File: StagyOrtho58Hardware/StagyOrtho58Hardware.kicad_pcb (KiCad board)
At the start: 2 copper layers, 73 parts, among them J11 USB_C_Receptacle, SW11 SW_Push, SW12 SW_Push, SW13 SW_Push, SW14 SW_Push, SW15 SW_Push, SW16 SW_Push, SW17 SW_Push, SW18 SW_Push, SW19 SW_Push, SW20 SW_Push, SW21 SW_Push, SW22 SW_Push, SW23 SW_Push, SW24 SW_Push, SW25 SW_Push, SW26 SW_Push, SW27 SW_Push, SW28 SW_Push, SW29 SW_Push, SW30 SW_Push, SW31 SW_Push, SW32 SW_Push, SW33 SW_Push, SW34 SW_Push, SW35 SW_Push, SW36 SW_Push, SW37 SW_Push, SW38 SW_Push, SW39 SW_Push, SW40 SW_Push, U11 Pico, U12 MCP23S17_ML

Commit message: Comfortable positions of the keys, ready to layout
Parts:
- J11: value USB_C_Receptacle -> USB_C_Receptacle_USB2.0
- SW29: footprint Switch_Keyboard_Kailh:SW_Kailh_Choc_V1V2_1.50u -> Switch_Keyboard_Kailh:SW_Kailh_Choc_V1V2_2.00u
- SW35: footprint Switch_Keyboard_Kailh:SW_Kailh_Choc_V1V2_1.50u -> Switch_Keyboard_Kailh:SW_Kailh_Choc_V1V2_1.00u
- SW38: footprint Switch_Keyboard_Kailh:SW_Kailh_Choc_V1V2_1.50u_90deg -> Switch_Keyboard_Kailh:SW_Kailh_Choc_V1V2_1.50u
- SW39: footprint Switch_Keyboard_Kailh:SW_Kailh_Choc_V1V2_2.00u -> Switch_Keyboard_Kailh:SW_Kailh_Choc_V1V2_1.00u
- moved SW34 69.9 mm to (144.1, 135.4)
- moved SW30 42.8 mm to (153.7, 112.0)
- moved SW38 36.6 mm to (233.2, 145.8), turned to 35 degrees
- moved SW39 30.0 mm to (231.1, 105.9)
- moved SW37 28.3 mm to (222.8, 130.8), turned to 35 degrees
- moved SW35 26.0 mm to (170.2, 135.4)
- moved SW36 24.8 mm to (194.9, 135.4)
- moved SW31 23.7 mm to (172.7, 108.2)
- moved SW32 21.9 mm to (191.8, 114.3)
- moved SW33 21.0 mm to (210.8, 111.5)
- moved SW29 16.3 mm to (120.4, 117.1)
- moved J11 12.6 mm to (55.9, 99.7)
- moved SW11 11.7 mm to (115.6, 62.2)
- moved SW17 7.08 mm to (111.0, 80.5)
- moved SW23 6.93 mm to (111.0, 98.8)
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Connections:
- J11 pad A5: unconnected-(J11-PadA5) -> /~{RESET}
- J11 pad A8: unconnected-(J11-PadA8) -> Net-(U12-Pad15)
- J11 pad B5: unconnected-(J11-PadB5) -> /GREEN
- J11 pad B8: unconnected-(J11-PadB8) -> Net-(U12-Pad16)
- U12 pad 14: Net-(J11-PadA3) -> /~{RESET}
- U12 pad 15: Net-(J11-PadB10) -> Net-(U12-Pad15)
- U12 pad 16: Net-(J11-PadB11) -> Net-(U12-Pad16)

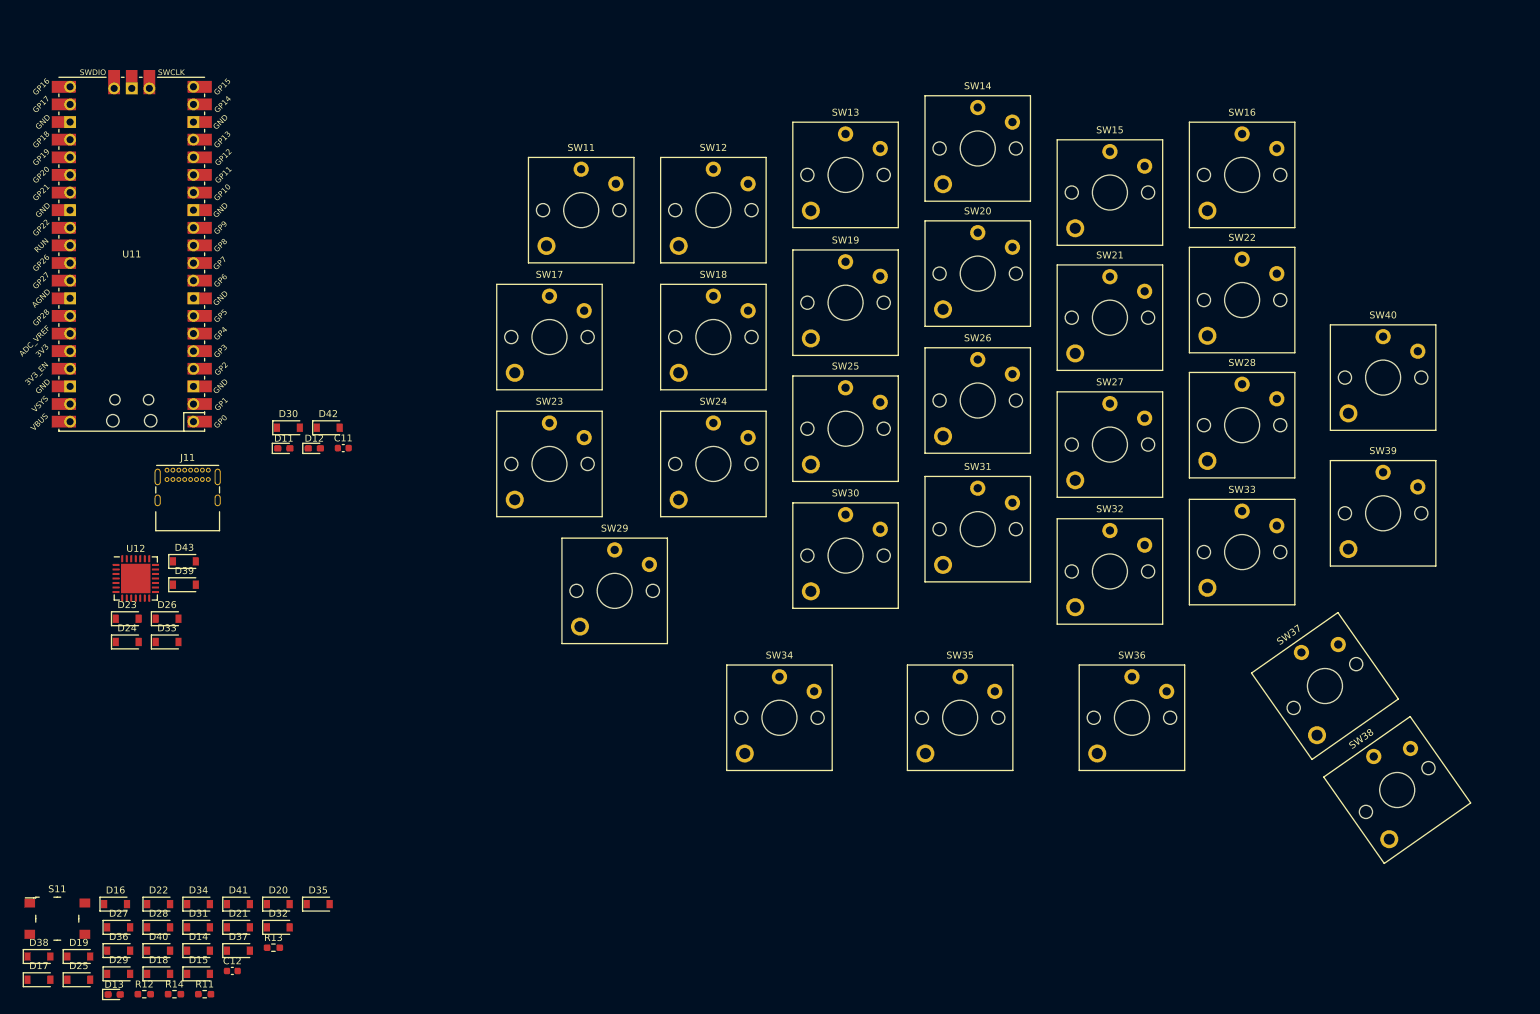
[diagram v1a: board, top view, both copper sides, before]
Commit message: Placed all components, board outline added
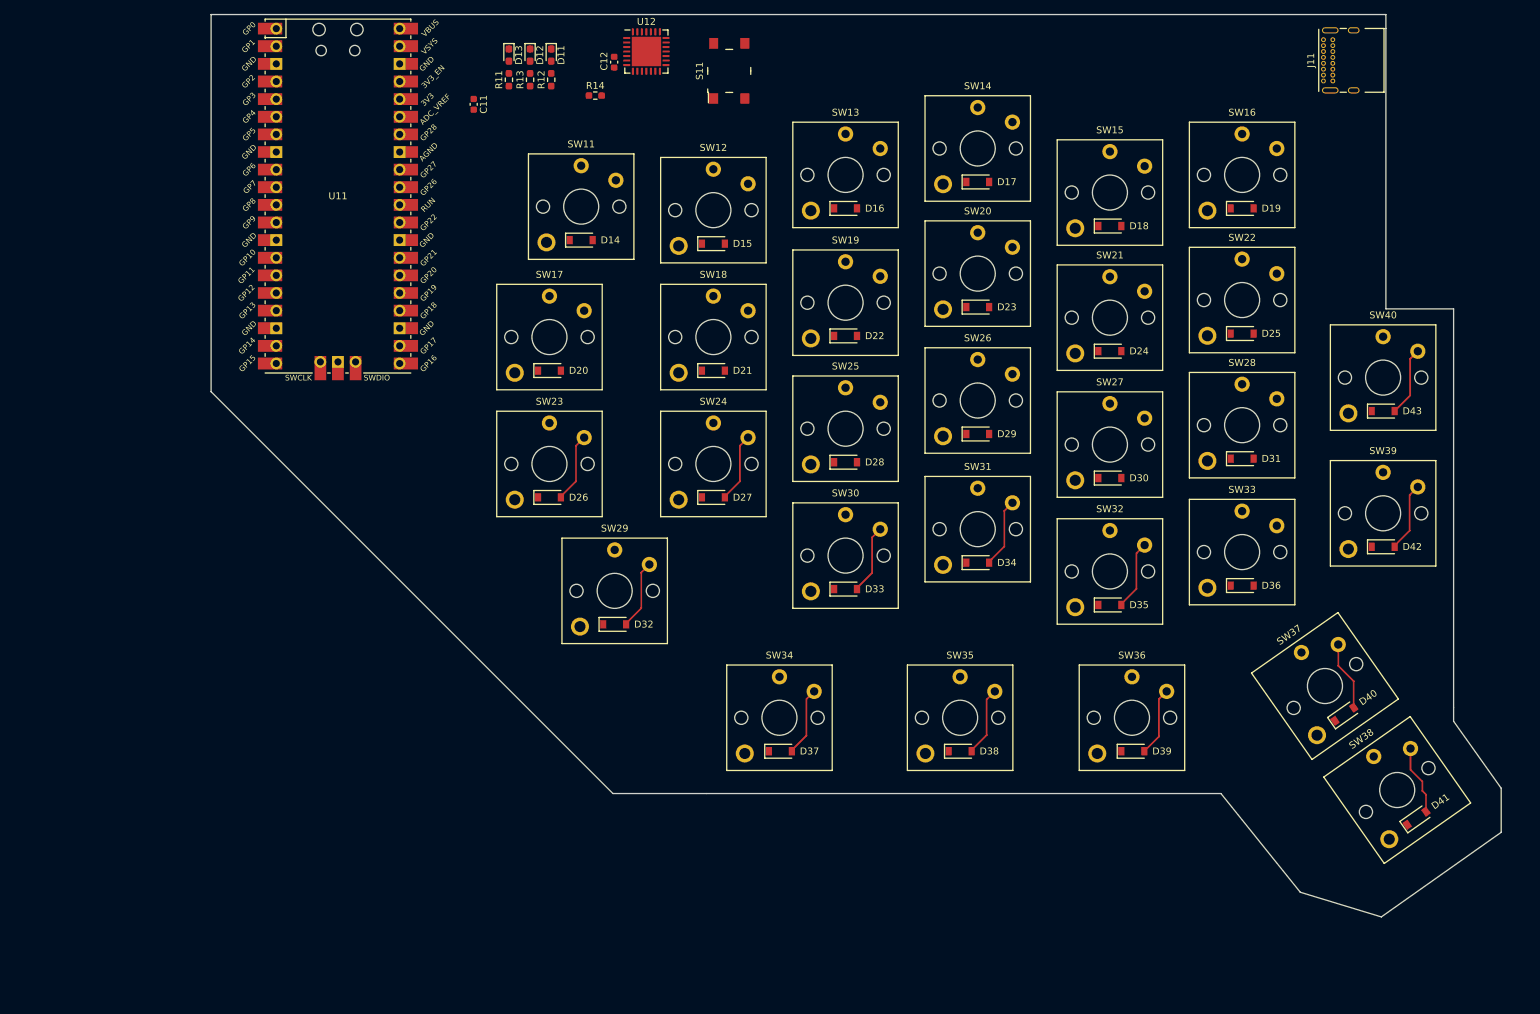
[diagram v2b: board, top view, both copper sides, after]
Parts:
- SW37, SW38: footprint Switch_Keyboard_Kailh:SW_Kailh_Choc_V1V2_1.50u -> Switch_Keyboard_Kailh:SW_Kailh_Choc_V1V2_1.00u
- moved D19 199.3 mm to (210.8, 62.0)
- moved D25 191.8 mm to (210.8, 80.0)
- moved D17 177.6 mm to (172.7, 58.2)
- moved J11 175.8 mm to (222.5, 43.6), turned to 90 degrees
- moved D18 174.4 mm to (191.8, 64.5)
- moved D40 174.2 mm to (225.6, 134.9), turned to 35 degrees
- moved D43 174.1 mm to (231.1, 91.2)
- moved D41 170.3 mm to (236.0, 149.9), turned to 35 degrees
- moved D36 170.2 mm to (210.8, 116.3)
- moved D31 164.9 mm to (210.8, 98.0)
- moved S11 155.9 mm to (136.9, 42.2), turned to 90 degrees
- moved D42 153.0 mm to (231.1, 110.7)
- moved D24 147.7 mm to (191.8, 82.5)
- moved D13 146.9 mm to (105.2, 39.9), turned to -90 degrees
- moved D29 146.2 mm to (172.7, 94.5)
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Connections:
- net Net-(U12-Pad15) renamed /INTB
- net Net-(U12-Pad16) renamed /INTA
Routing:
- net Net-(D41-Pad2): track 0.00 -> 10.0 mm
- net Net-(D40-Pad2): track 0.00 -> 10.0 mm
- net Net-(D35-Pad2): track 0.00 -> 10.0 mm
- net Net-(D26-Pad2): track 0.00 -> 10.0 mm
- net Net-(D42-Pad2): track 0.00 -> 10.0 mm
- net Net-(D38-Pad2): track 0.00 -> 10.0 mm
- net Net-(D34-Pad2): track 0.00 -> 10.0 mm
- net Net-(D33-Pad2): track 0.00 -> 10.0 mm
- net Net-(D32-Pad2): track 0.00 -> 10.0 mm
- net Net-(D43-Pad2): track 0.00 -> 10.0 mm
- net Net-(D27-Pad2): track 0.00 -> 10.0 mm
- net Net-(D37-Pad2): track 0.00 -> 9.96 mm
- net Net-(D39-Pad2): track 0.00 -> 9.96 mm
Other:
- board outline added: 185.9 x 130 mm

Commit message: Partial routing complete, approx 40%
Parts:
- added H11: MountingHole, MountingHole:MountingHole_3.2mm_M3, F.Cu at (66.0, 86.4)
- added H12: MountingHole, MountingHole:MountingHole_3.2mm_M3, F.Cu at (123.0, 140.4)
- added H13: MountingHole, MountingHole:MountingHole_3.2mm_M3, F.Cu at (236.4, 119.6)
- added H14: MountingHole, MountingHole:MountingHole_3.2mm_M3, F.Cu at (157.9, 38.2)
- added H15: MountingHole, MountingHole:MountingHole_3.2mm_M3, F.Cu at (226.6, 51.9)
- added H16: MountingHole, MountingHole:MountingHole_3.2mm_M3, F.Cu at (65.7, 37.8)
- added H17: MountingHole, MountingHole:MountingHole_2.7mm_M2.5, F.Cu at (207.2, 124.3)
- added H18: MountingHole, MountingHole:MountingHole_2.7mm_M2.5, F.Cu at (122.7, 73.9)
- added H19: MountingHole, MountingHole:MountingHole_2.7mm_M2.5, F.Cu at (168.3, 85.4)
- added H20: MountingHole, MountingHole:MountingHole_2.7mm_M2.5, F.Cu at (171.7, 121.0)
- SW37: footprint Switch_Keyboard_Kailh:SW_Kailh_Choc_V1V2_1.00u -> Switch_Keyboard_Kailh:SW_Kailh_Choc_V1V2_1.50u
- moved D37 9.74 mm to (154.0, 139.8)
- moved SW34 9.74 mm to (153.9, 135.0)
- moved D41 4.58 mm to (232.7, 153.1)
- moved SW38 4.58 mm to (229.9, 149.0)
- moved SW35 4.50 mm to (174.7, 135.0)
- moved D38 4.50 mm to (174.7, 139.8)
- moved SW37 1.10 mm to (221.7, 131.1)
- moved D40 1.10 mm to (224.5, 135.2)
- moved U11 1.08 mm to (81.6, 60.2)
- moved SW36 0.49 mm to (195.2, 135.0)
- moved D39 0.49 mm to (195.3, 139.8)
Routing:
- net /ROW_4: track 0.00 -> 135.6 mm
- net /ROW_3: track 0.00 -> 132.4 mm
- net /ROW_2: track 0.00 -> 122.4 mm
- net /ROW_1: track 0.00 -> 122.0 mm
- net /ROW_0: track 0.00 -> 118.6 mm
- net /COL_0: track 0.00 -> 72.2 mm
- net /COL_5: track 0.00 -> 62.5 mm
- net /COL_2: track 0.00 -> 42.6 mm
- net /COL_1: track 0.00 -> 42.6 mm
- net /COL_4: track 0.00 -> 42.3 mm
- net /COL_3: track 0.00 -> 42.2 mm
- net Net-(D18-Pad2): track 0.00 -> 10.0 mm
- net Net-(D24-Pad2): track 0.00 -> 10.0 mm
- net Net-(D30-Pad2): track 0.00 -> 10.0 mm
- net Net-(D29-Pad2): track 0.00 -> 10.0 mm
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
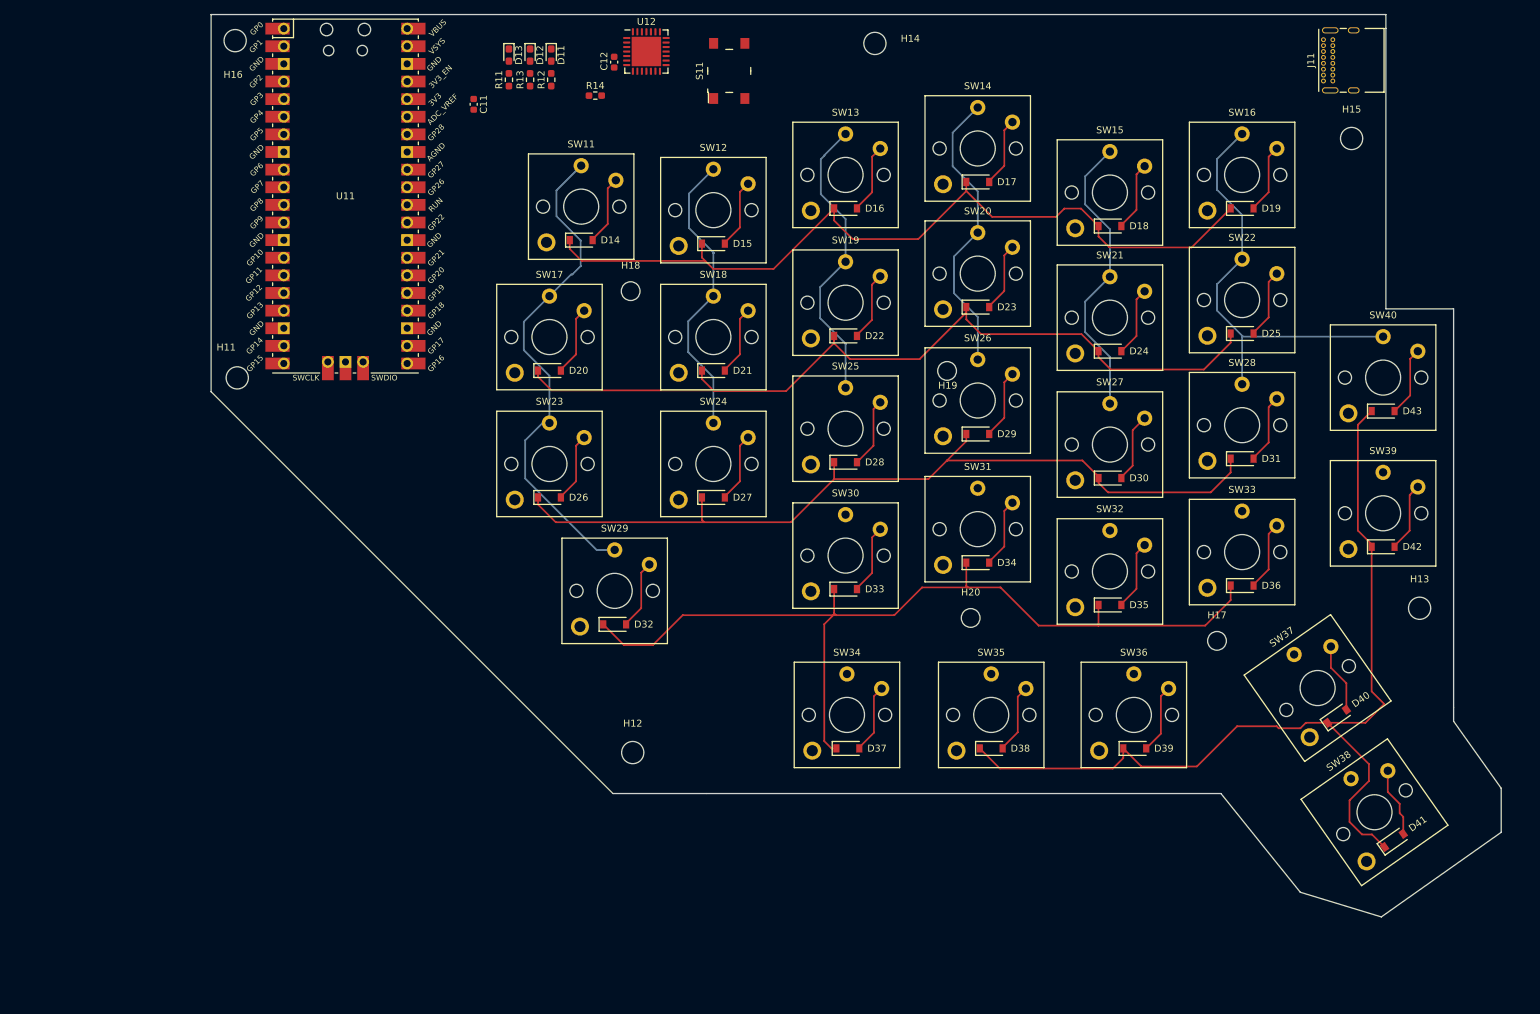
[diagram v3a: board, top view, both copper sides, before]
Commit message: Routes rows, columns in switches
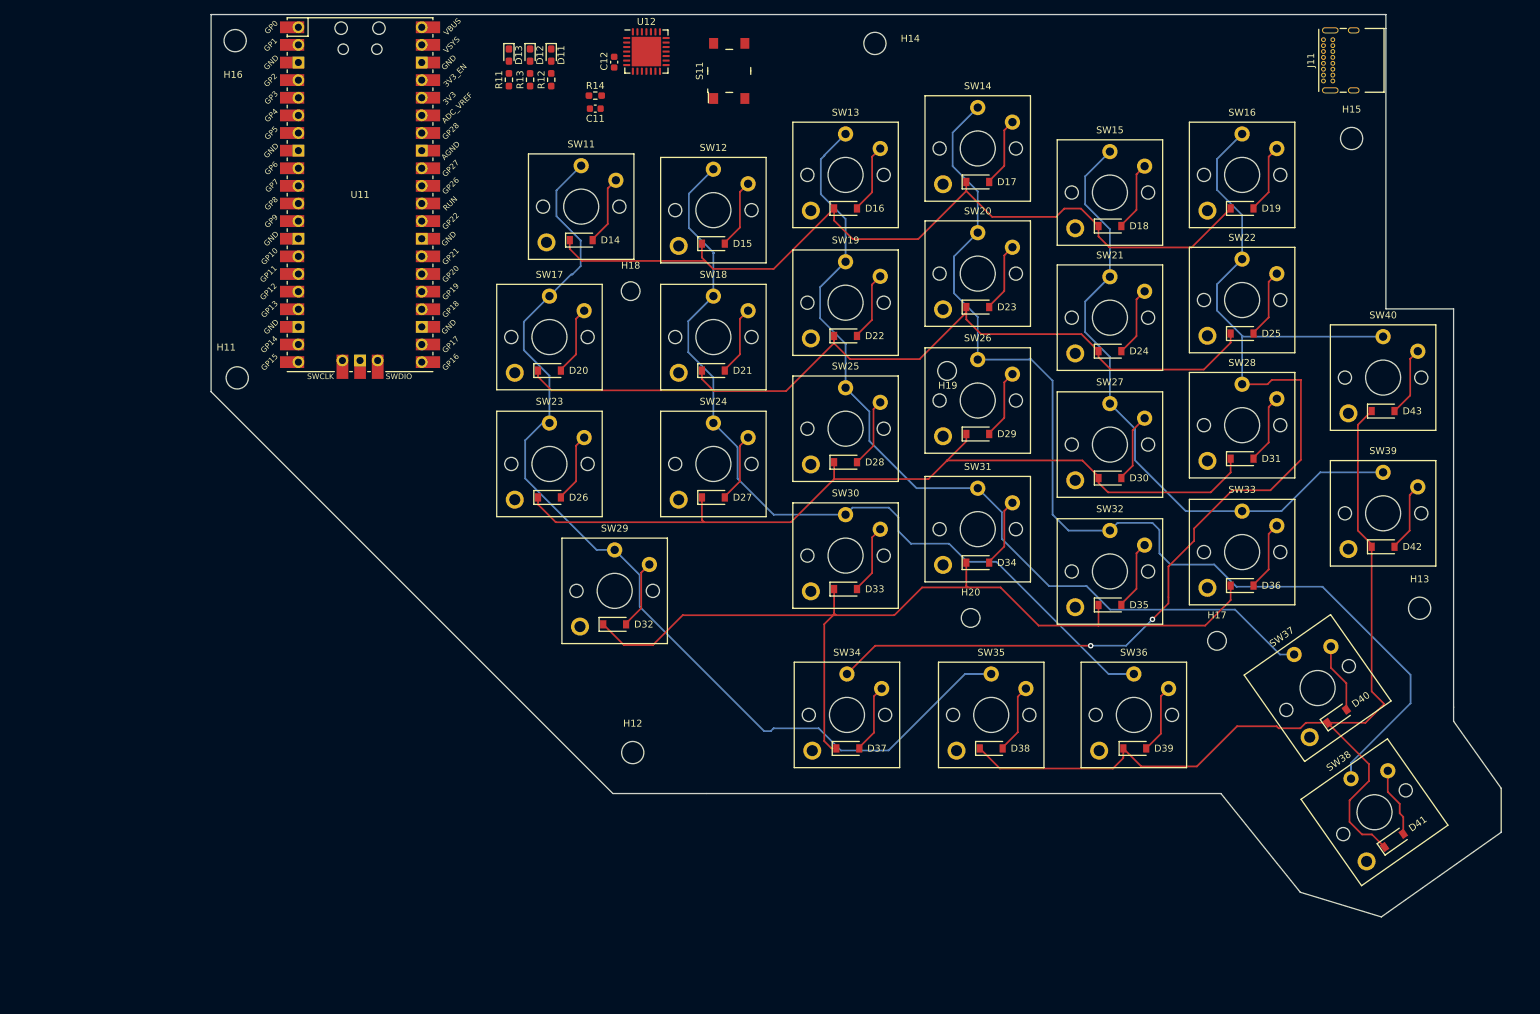
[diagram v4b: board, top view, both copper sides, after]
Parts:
- moved C11 17.5 mm to (117.6, 47.6), turned to 180 degrees
- moved U11 2.11 mm to (83.7, 60.0)
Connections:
- C12 pad 2: GNDD -> GND
- J11 pad A1: GNDD -> GND
- J11 pad A12: GNDD -> GND
- J11 pad B1: GNDD -> GND
- J11 pad B12: GNDD -> GND
- J11 pad S1: GNDD -> GND
- U12 pad 11: GNDD -> GND
- U12 pad 12: GNDD -> GND
- U12 pad 13: GNDD -> GND
- U12 pad 29: GNDD -> GND
- U12 pad 6: GNDD -> GND
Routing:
- net /COL_3: track 42.2 -> 156.2 mm
- net /COL_5: track 62.5 -> 165.1 mm, vias 0 -> 2
- net /COL_2: track 42.6 -> 127.9 mm
- net /COL_1: track 42.6 -> 122.8 mm
- net /COL_0: track 72.2 -> 146.1 mm
- net /COL_4: track 42.3 -> 93.0 mm
